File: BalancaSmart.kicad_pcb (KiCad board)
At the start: 2 copper layers, 7 parts, among them J1 Load Cell, Q4 S8050, SW1 SW_Push, U1 HX711-Mod

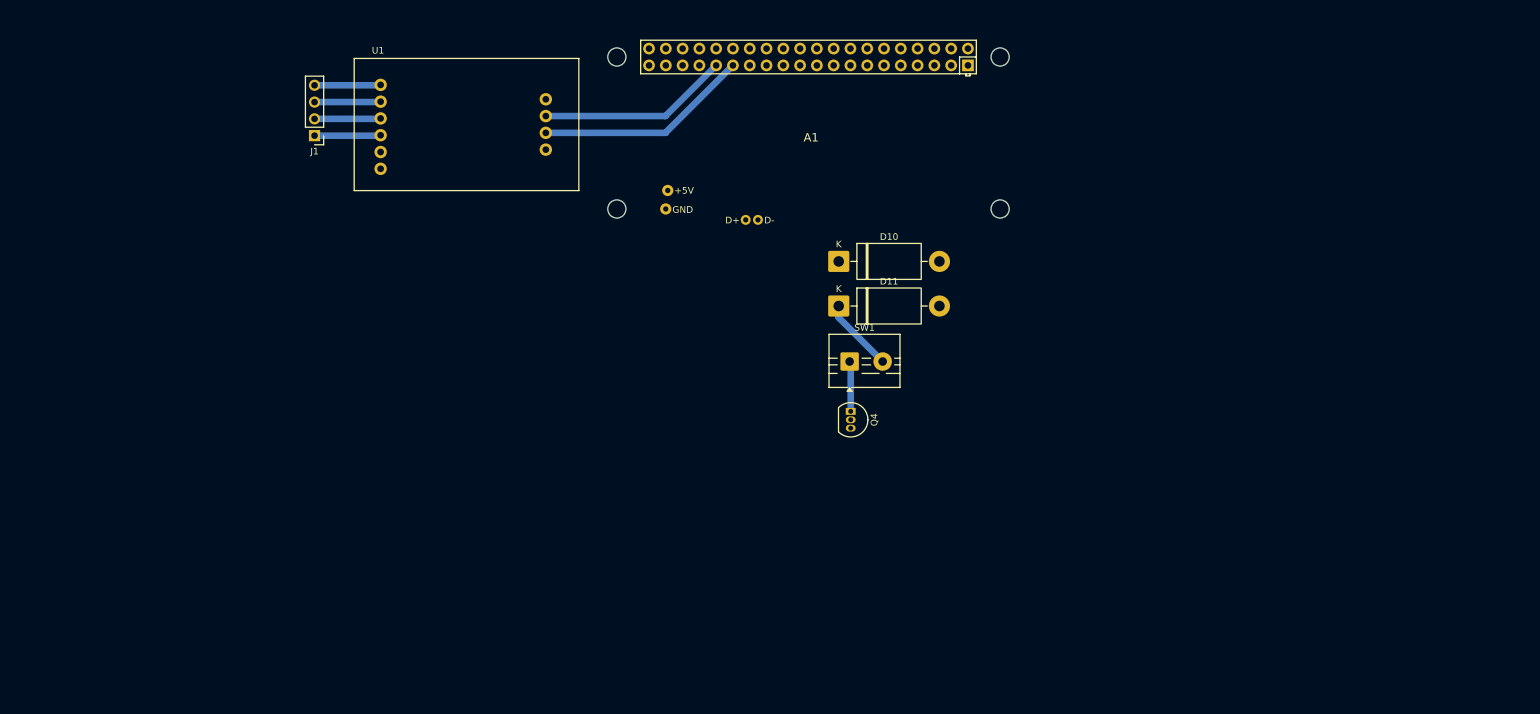
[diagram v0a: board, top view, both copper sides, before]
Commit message: adicionado footprint do ADS1115, continuação do desenvolvimento do layout da pcb
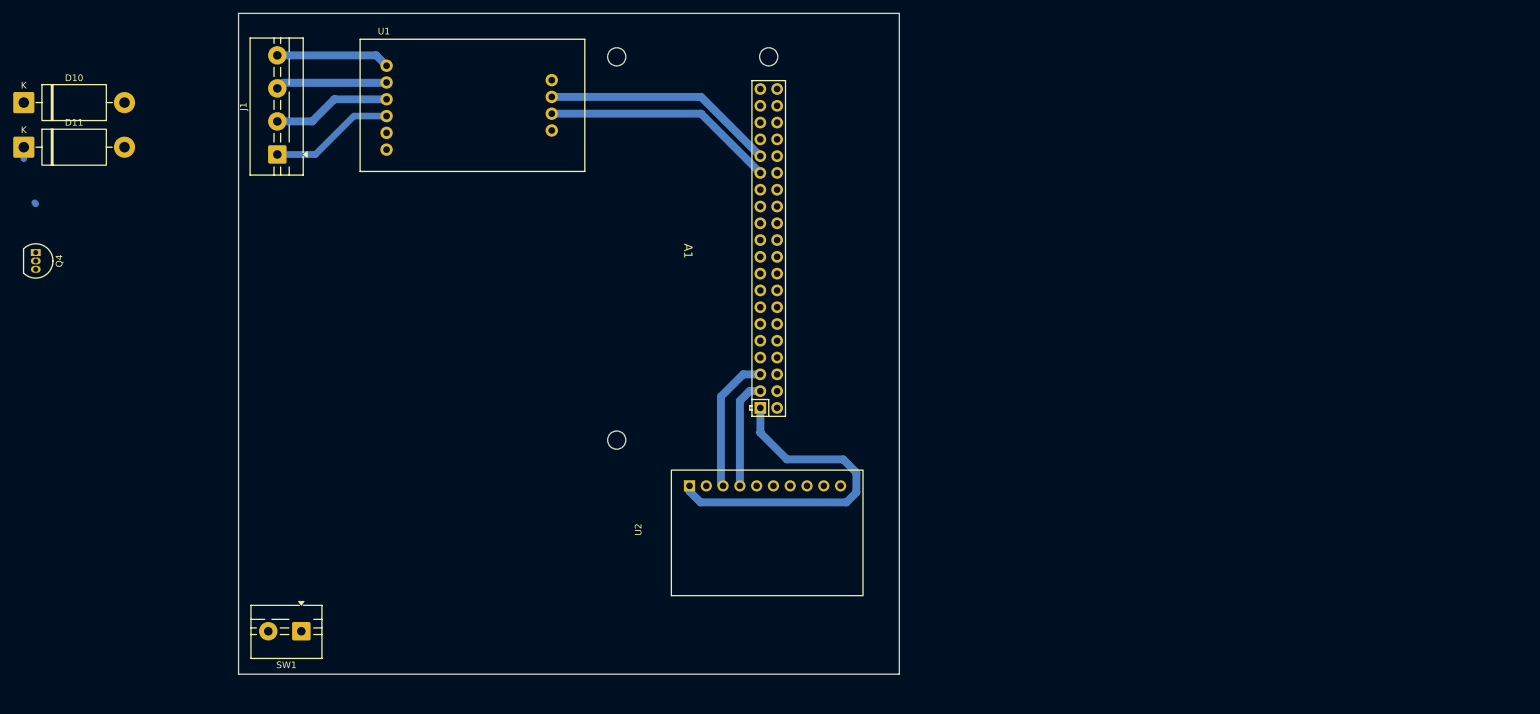
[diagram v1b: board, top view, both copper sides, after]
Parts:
- added U2: ADS1115-module, project_library:ADS1115 Module, F.Cu at (123.5, 150.1)
- J1: footprint Connector_PinHeader_2.54mm:PinHeader_1x04_P2.54mm_Vertical -> TerminalBlock:TerminalBlock_MaiXu_MX126-5.0-04P_1x04_P5.00mm
- moved D10 125.6 mm to (30.0, 85.5)
- moved D11 125.6 mm to (30.0, 92.2)
- moved Q4 125.6 mm to (31.8, 108.2)
- moved SW1 92.5 mm to (72.0, 165.5), turned to 180 degrees
- moved A1 30.0 mm to (116.2, 75.1), turned to -90 degrees
- moved J1 6.31 mm to (68.4, 93.3), turned to 90 degrees
- moved U1 3.04 mm to (97.9, 85.9)
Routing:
- net +3V3: track 0.00 -> 51.2 mm
- net I2C SCL: track 0.00 -> 21.0 mm
- net I2C SDA: track 0.00 -> 16.6 mm
- net Net-(D11-K): track 11.2 -> 1.75 mm
- net Net-(J1-Pin_1): track 10.0 -> 19.0 mm
- net Net-(J1-Pin_2): track 10.0 -> 18.0 mm
- net Earth: track 7.61 -> 0.23 mm
- net Net-(J1-Pin_4): track 10.0 -> 17.2 mm
- net Net-(J1-Pin_3): track 10.0 -> 17.0 mm
- net DAT HX711: track 29.0 -> 35.3 mm
- net CLK HX711: track 32.5 -> 35.3 mm
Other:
- board outline added: 100 x 100 mm

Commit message: designação de footprints
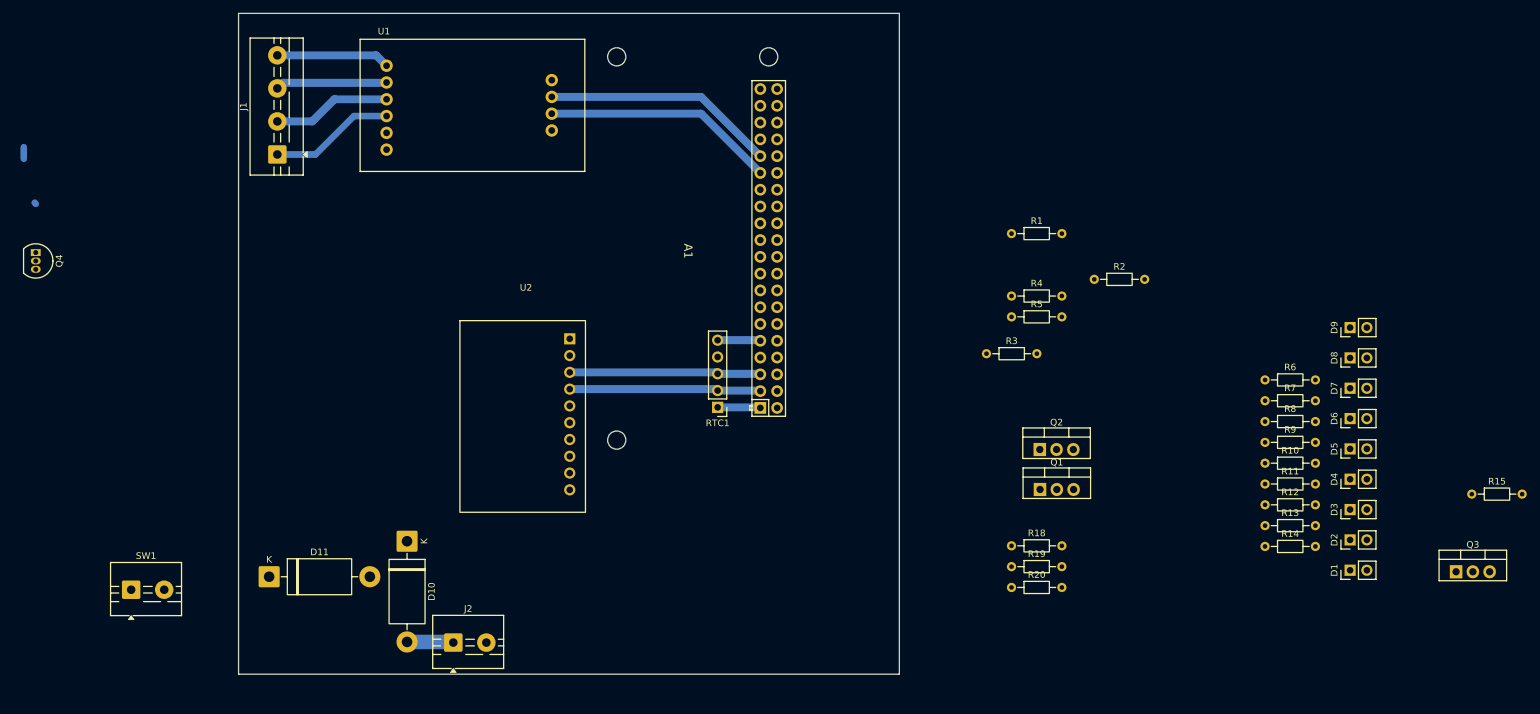
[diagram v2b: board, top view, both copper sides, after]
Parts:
- added D1: LED, Connector_PinHeader_2.54mm:PinHeader_1x02_P2.54mm_Vertical, F.Cu at (230.7, 156.3)
- added D2: LED, Connector_PinHeader_2.54mm:PinHeader_1x02_P2.54mm_Vertical, F.Cu at (230.7, 151.7)
- added D3: LED, Connector_PinHeader_2.54mm:PinHeader_1x02_P2.54mm_Vertical, F.Cu at (230.7, 147.1)
- added D4: LED, Connector_PinHeader_2.54mm:PinHeader_1x02_P2.54mm_Vertical, F.Cu at (230.7, 142.5)
- added D5: LED, Connector_PinHeader_2.54mm:PinHeader_1x02_P2.54mm_Vertical, F.Cu at (230.7, 137.9)
- added D6: LED, Connector_PinHeader_2.54mm:PinHeader_1x02_P2.54mm_Vertical, F.Cu at (230.7, 133.3)
- added D7: LED, Connector_PinHeader_2.54mm:PinHeader_1x02_P2.54mm_Vertical, F.Cu at (230.7, 128.7)
- added D8: LED, Connector_PinHeader_2.54mm:PinHeader_1x02_P2.54mm_Vertical, F.Cu at (230.7, 124.1)
- added D9: LED, Connector_PinHeader_2.54mm:PinHeader_1x02_P2.54mm_Vertical, F.Cu at (230.7, 119.5)
- added J2: Barrel_Jack, TerminalBlock:TerminalBlock_MaiXu_MX126-5.0-02P_1x02_P5.00mm, F.Cu at (95.0, 167.2)
- added Q1: PMOS, Package_TO_SOT_THT:TO-220-3_Vertical, F.Cu at (183.8, 144.1)
- added Q2: NMOS, Package_TO_SOT_THT:TO-220-3_Vertical, F.Cu at (183.8, 138.0)
- added Q3: NMOS, Package_TO_SOT_THT:TO-220-3_Vertical, F.Cu at (246.8, 156.5)
- added R1: 10k, Resistor_THT:R_Axial_DIN0204_L3.6mm_D1.6mm_P7.62mm_Horizontal, F.Cu at (179.5, 105.3)
- added R10: 100, Resistor_THT:R_Axial_DIN0204_L3.6mm_D1.6mm_P7.62mm_Horizontal, F.Cu at (217.8, 140.1)
- added R11: 100, Resistor_THT:R_Axial_DIN0204_L3.6mm_D1.6mm_P7.62mm_Horizontal, F.Cu at (217.8, 143.2)
- added R12: 100, Resistor_THT:R_Axial_DIN0204_L3.6mm_D1.6mm_P7.62mm_Horizontal, F.Cu at (217.8, 146.4)
- added R13: 100, Resistor_THT:R_Axial_DIN0204_L3.6mm_D1.6mm_P7.62mm_Horizontal, F.Cu at (217.8, 149.5)
- added R14: 100, Resistor_THT:R_Axial_DIN0204_L3.6mm_D1.6mm_P7.62mm_Horizontal, F.Cu at (217.8, 152.7)
- added R15: 1k, Resistor_THT:R_Axial_DIN0204_L3.6mm_D1.6mm_P7.62mm_Horizontal, F.Cu at (249.1, 144.8)
- added R18: 1k, Resistor_THT:R_Axial_DIN0204_L3.6mm_D1.6mm_P7.62mm_Horizontal, F.Cu at (179.5, 152.6)
- added R19: 100k, Resistor_THT:R_Axial_DIN0204_L3.6mm_D1.6mm_P7.62mm_Horizontal, F.Cu at (179.5, 155.7)
- added R2: 100k, Resistor_THT:R_Axial_DIN0204_L3.6mm_D1.6mm_P7.62mm_Horizontal, F.Cu at (192.0, 112.2)
- added R20: 56k, Resistor_THT:R_Axial_DIN0204_L3.6mm_D1.6mm_P7.62mm_Horizontal, F.Cu at (179.5, 158.9)
- added R3: 100k, Resistor_THT:R_Axial_DIN0204_L3.6mm_D1.6mm_P7.62mm_Horizontal, F.Cu at (175.7, 123.5)
- added R4: 300k, Resistor_THT:R_Axial_DIN0204_L3.6mm_D1.6mm_P7.62mm_Horizontal, F.Cu at (179.5, 114.8)
- added R5: 1k, Resistor_THT:R_Axial_DIN0204_L3.6mm_D1.6mm_P7.62mm_Horizontal, F.Cu at (179.5, 117.9)
- added R6: 100, Resistor_THT:R_Axial_DIN0204_L3.6mm_D1.6mm_P7.62mm_Horizontal, F.Cu at (217.8, 127.5)
- added R7: 100, Resistor_THT:R_Axial_DIN0204_L3.6mm_D1.6mm_P7.62mm_Horizontal, F.Cu at (217.8, 130.6)
- added R8: 100, Resistor_THT:R_Axial_DIN0204_L3.6mm_D1.6mm_P7.62mm_Horizontal, F.Cu at (217.8, 133.8)
- added R9: 100, Resistor_THT:R_Axial_DIN0204_L3.6mm_D1.6mm_P7.62mm_Horizontal, F.Cu at (217.8, 136.9)
- added RTC1: RTC_DS3231, Connector_PinHeader_2.54mm:PinHeader_1x05_P2.54mm_Vertical, F.Cu at (135.0, 131.6)
- moved D10 88.1 mm to (88.0, 151.9), turned to -90 degrees
- moved D11 74.9 mm to (67.1, 157.2)
- moved U2 40.1 mm to (106.0, 114.0), turned to 0 degrees
- moved SW1 26.5 mm to (46.2, 159.2), turned to 0 degrees
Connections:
- A1 pad 9: unconnected-(A1-GND-Pad9) -> Earth
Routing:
- net +3V3: track 51.2 -> 6.50 mm
- net I2C SDA: track 16.6 -> 29.0 mm
- net I2C SCL: track 21.0 -> 29.0 mm
- net Net-(D10-A): track 0.00 -> 7.04 mm
- net Earth: track 0.23 -> 6.73 mm

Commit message: layout do circuito dos leds
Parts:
- moved D11 137.9 mm to (187.8, 90.5)
- moved R15 114.8 mm to (142.7, 101.8), turned to 90 degrees
- moved Q3 112.1 mm to (151.3, 97.8)
- moved D1 90.8 mm to (157.3, 102.8), turned to -90 degrees
- moved D2 85.7 mm to (157.3, 107.4), turned to -90 degrees
- moved R14 82.6 mm to (149.9, 105.7), turned to 180 degrees
- moved D3 81.4 mm to (157.3, 112.0), turned to -90 degrees
- moved R13 79.2 mm to (149.9, 108.8), turned to 180 degrees
- moved D4 77.8 mm to (157.3, 116.6), turned to -90 degrees
- moved R12 76.1 mm to (149.9, 112.0), turned to 180 degrees
- moved D9 76.1 mm to (157.3, 139.5), turned to -90 degrees
- moved D5 75.3 mm to (157.3, 121.2), turned to -90 degrees
- moved D8 74.2 mm to (157.3, 134.9), turned to -90 degrees
- moved D6 73.8 mm to (157.3, 125.8), turned to -90 degrees
- moved R11 73.5 mm to (149.9, 115.1), turned to 180 degrees
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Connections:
- R10 pad 1: +5V -> Net-(D5-A)
- R10 pad 2: Net-(D5-A) -> +5V
- R11 pad 1: +5V -> Net-(D4-A)
- R11 pad 2: Net-(D4-A) -> +5V
- R12 pad 1: +5V -> Net-(D3-A)
- R12 pad 2: Net-(D3-A) -> +5V
- R13 pad 1: +5V -> Net-(D2-A)
- R13 pad 2: Net-(D2-A) -> +5V
- R14 pad 1: +5V -> Net-(D1-A)
- R14 pad 2: Net-(D1-A) -> +5V
- R6 pad 1: +5V -> Net-(D9-A)
- R6 pad 2: Net-(D9-A) -> +5V
- R7 pad 1: +5V -> Net-(D8-A)
- R7 pad 2: Net-(D8-A) -> +5V
- R8 pad 1: +5V -> Net-(D7-A)
- R8 pad 2: Net-(D7-A) -> +5V
- R9 pad 1: +5V -> Net-(D6-A)
- R9 pad 2: Net-(D6-A) -> +5V
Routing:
- net Net-(D1-K): track 0.00 -> 75.3 mm
- net +5V: track 0.00 -> 44.3 mm
- net I2C SCL: track 29.0 -> 0.30 mm
- net I2C SDA: track 29.0 -> 0.30 mm
- net Net-(Q3-G): track 0.00 -> 15.1 mm
- net Net-(D9-A): track 0.00 -> 12.6 mm
- net Net-(D8-A): track 0.00 -> 10.3 mm
- net Net-(D7-A): track 0.00 -> 7.81 mm
- net Net-(J1-Pin_2): track 18.0 -> 11.0 mm
- net Net-(J1-Pin_3): track 17.0 -> 10.0 mm
- net Net-(J1-Pin_1): track 19.0 -> 12.0 mm
- net Net-(J1-Pin_4): track 17.2 -> 10.3 mm
- net Net-(D6-A): track 0.00 -> 6.63 mm
- net Earth: track 6.73 -> 0.23 mm
- net +3V3: track 6.50 -> 0.00 mm
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
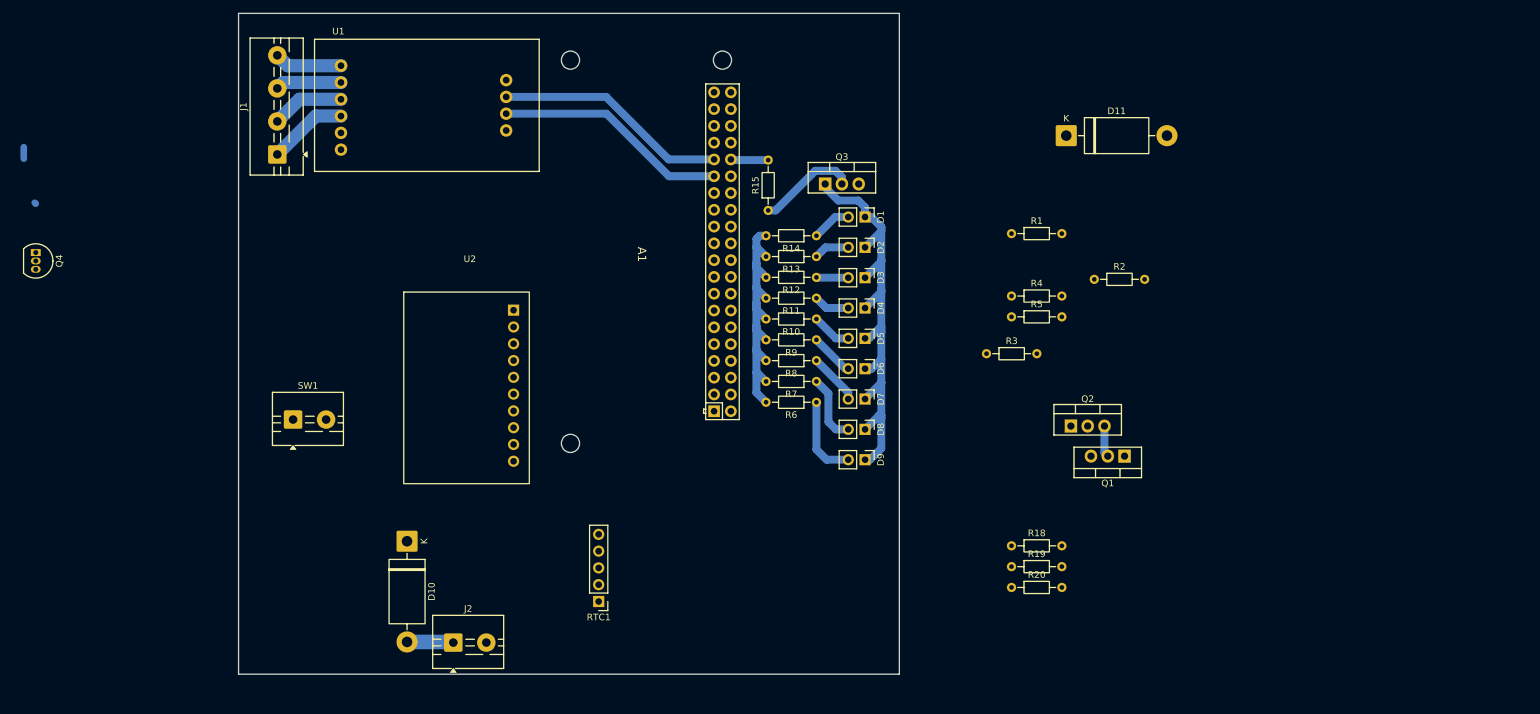
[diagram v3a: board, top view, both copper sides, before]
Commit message: continuação do layout da PCB e designação de footprints
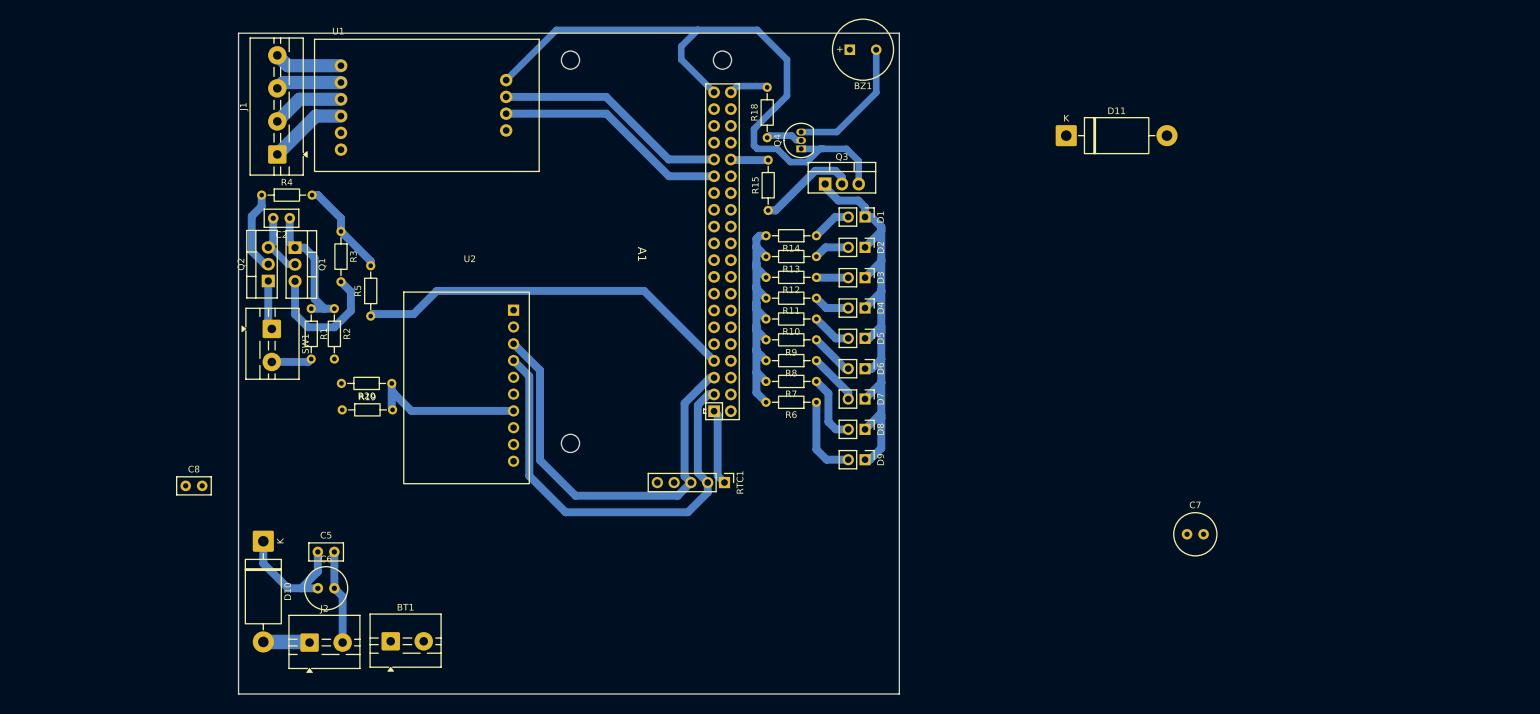
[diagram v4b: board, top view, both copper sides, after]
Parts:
- added BT1: Battery, TerminalBlock:TerminalBlock_MaiXu_MX126-5.0-02P_1x02_P5.00mm, F.Cu at (85.5, 167.0)
- added BZ1: Buzzer, Buzzer_Beeper:MagneticBuzzer_PUI_AT-0927-TT-6-R, F.Cu at (155.0, 77.5)
- added C2: 0.1uF, Capacitor_THT:C_Disc_D5.0mm_W2.5mm_P2.50mm, F.Cu at (70.2, 103.0)
- added C5: 100nF, Capacitor_THT:C_Disc_D5.0mm_W2.5mm_P2.50mm, F.Cu at (74.5, 153.5)
- added C6: 470uF, Capacitor_THT:C_Radial_D6.3mm_H7.0mm_P2.50mm, F.Cu at (74.5, 159.0)
- added C7: 220uF, Capacitor_THT:C_Radial_D6.3mm_H7.0mm_P2.50mm, F.Cu at (206.0, 150.8)
- added C8: 100nF, Capacitor_THT:C_Disc_D5.0mm_W2.5mm_P2.50mm, F.Cu at (54.5, 143.5)
- moved Q1 129.4 mm to (71.0, 107.5), turned to -90 degrees
- moved Q2 123.4 mm to (67.0, 112.5), turned to 90 degrees
- moved Q4 116.9 mm to (147.6, 92.5), turned to 90 degrees
- moved R2 115.1 mm to (77.0, 116.7), turned to -90 degrees
- moved R4 114.5 mm to (66.0, 99.5)
- moved R1 106.6 mm to (73.5, 116.7), turned to -90 degrees
- moved R19 104.0 mm to (78.2, 132.0)
- moved R3 99.4 mm to (78.0, 105.0), turned to -90 degrees
- moved R20 98.7 mm to (85.7, 128.0), turned to 180 degrees
- moved R5 97.0 mm to (82.5, 117.8), turned to 90 degrees
- moved R18 72.0 mm to (142.5, 90.8), turned to 90 degrees
- moved RTC1 26.2 mm to (136.0, 143.0), turned to -90 degrees
- moved D10 21.8 mm to (66.2, 151.9)
- moved J2 21.8 mm to (73.2, 167.2)
- moved SW1 14.1 mm to (67.5, 119.8), turned to -90 degrees
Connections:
- A1 pad 33: Buzzer -> unconnected-(A1-GP13/PWM1-Pad33)
- A1 pad 40: unconnected-(A1-GP21-Pad40) -> Buzzer
- D10 pad 1: Net-(D10-K) -> P+
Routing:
- net Earth: track 0.23 -> 107.9 mm
- net I2C SDA: track 0.30 -> 65.9 mm
- net I2C SCL: track 0.30 -> 63.6 mm
- net Sinal de desligamento: track 0.00 -> 57.9 mm
- net Net-(U2-A0): track 0.00 -> 23.6 mm
- net Net-(BZ1--): track 0.00 -> 20.3 mm
- net pino 5v rasp: track 0.00 -> 20.3 mm
- net +5V: track 44.3 -> 64.5 mm
- net P+: track 0.00 -> 19.7 mm
- net Net-(D11-A): track 0.00 -> 14.9 mm
- net P-: track 0.00 -> 14.2 mm
- net Net-(Q2-G): track 0.00 -> 12.4 mm
- net +3V3: track 0.00 -> 11.4 mm
- net Buzzer: track 0.00 -> 5.97 mm
- net Net-(Q4-B): track 0.00 -> 5.57 mm
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
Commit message: continuação pcb
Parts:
- added C1: 1uF, Capacitor_THT:C_Radial_D6.3mm_H7.0mm_P2.50mm, F.Cu at (66.0, 132.0)
- added C3: 10uF, Capacitor_THT:C_Radial_D6.3mm_H7.0mm_P2.50mm, F.Cu at (77.5, 112.5)
- added C4: 10uF, Capacitor_THT:C_Radial_D6.3mm_H7.0mm_P2.50mm, F.Cu at (144.0, 135.0)
- added C9: C, Capacitor_THT:C_Radial_D6.3mm_H7.0mm_P2.50mm, F.Cu at (83.5, 142.0)
- added U3: HX-2S-JH20, TerminalBlock:TerminalBlock_MaiXu_MX126-5.0-04P_1x04_P5.00mm, F.Cu at (149.0, 166.5)
- added U4: XL4015, TerminalBlock:TerminalBlock_MaiXu_MX126-5.0-04P_1x04_P5.00mm, F.Cu at (157.0, 167.5)
- moved D11 128.2 mm to (73.5, 148.6), turned to 90 degrees
- moved C8 88.8 mm to (142.5, 155.8), turned to 90 degrees
- moved C7 57.8 mm to (148.5, 156.0), turned to 90 degrees
- moved BT1 36.7 mm to (122.2, 166.5)
- moved C5 33.8 mm to (108.2, 156.0)
- moved C6 33.8 mm to (108.2, 161.5)
- moved D10 33.8 mm to (100.0, 154.4)
- moved J2 33.8 mm to (107.0, 169.7)
- moved R19 5.51 mm to (77.9, 137.5)
- moved R20 5.51 mm to (85.4, 133.5)
- moved R3 5.50 mm to (78.0, 99.5)
- moved R5 4.46 mm to (85.0, 121.5)
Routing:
- net P+: track 19.7 -> 109.5 mm
- net +5V: track 64.5 -> 128.9 mm
- net P-: track 14.2 -> 67.9 mm
- net Earth: track 107.9 -> 160.2 mm
- net Net-(D11-A): track 14.9 -> 50.6 mm
- net Net-(D11-K): track 6.15 -> 35.4 mm
- net Net-(Q2-G): track 12.4 -> 32.8 mm
- net Net-(BT1-+): track 0.00 -> 19.7 mm
- net pino 5v rasp: track 20.3 -> 32.2 mm
- net Net-(C1-Pad2): track 0.00 -> 11.7 mm
- net Net-(BT1--): track 0.00 -> 6.76 mm
- net Net-(U2-A0): track 23.6 -> 29.9 mm
- net Sinal de desligamento: track 57.9 -> 57.0 mm
